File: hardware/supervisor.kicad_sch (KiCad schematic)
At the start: 39 parts, among them U5 STM32L4P5RET6, U6 MCP2562-H-SN, Y1 Crystal_GND24

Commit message: Dimensions compress, routing
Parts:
- removed 120_JP1: Jumper_NC_Small, Jumper:SolderJumper-2_P1.3mm_Open_RoundedPad1.0x1.5mm, symbol Jumper:Jumper_2_Open
- removed C10, C12, C14, C15, C18, C7, C8, C9: 100nF, Capacitor_SMD:C_0603_1608Metric_Pad1.08x0.95mm_HandSolder, symbol Device:C
- removed C6: 1uF, Capacitor_SMD:C_0603_1608Metric_Pad1.08x0.95mm_HandSolder, symbol Device:C
- removed D2: PESD2CAN.215, Package_TO_SOT_SMD:SOT-23, symbol Device:D_TVS_Dual_AAC
- removed L1: 10u, Inductor_SMD:L_0805_2012Metric, symbol Device:L
- removed R13: 120R, Resistor_SMD:R_0603_1608Metric_Pad0.98x0.95mm_HandSolder, symbol Device:R_Small
- removed U6: MCP2562-H-SN, Package_SO:SOIC-8_3.9x4.9mm_P1.27mm, symbol Interface_CAN_LIN:MCP2562-H-SN
- Y1: value Crystal_GND24 -> 8MHz 3225 Crystal
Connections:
- net (CAN_RX)+ renamed CAN_RX
- net (CAN_TX)- renamed CAN_TX
- net XTAL1: no longer names the net of C11.1, U5.5 (PH0-OSC_IN), Y1.1
- net XTAL2: no longer names the net of C13.1, U5.6 (PH1-OSC_OUT), Y1.3
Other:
- added sheet CAN_comm (can.kicad_sch)
- added sheet uC power decoupling (decoupling.kicad_sch)
- note removed: "8Mhz"
- note removed: "sensor 1,2,3 Pins: 24, 25, 37"
- note removed: "those are just in case, brake pressure read from data acquisition card frames"
- note removed: "uC Power supply decoupling"
- moved on the sheet: C11, C13, D16, D17, D18, D6, JP1, JP2, R11, R12, R2, R20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

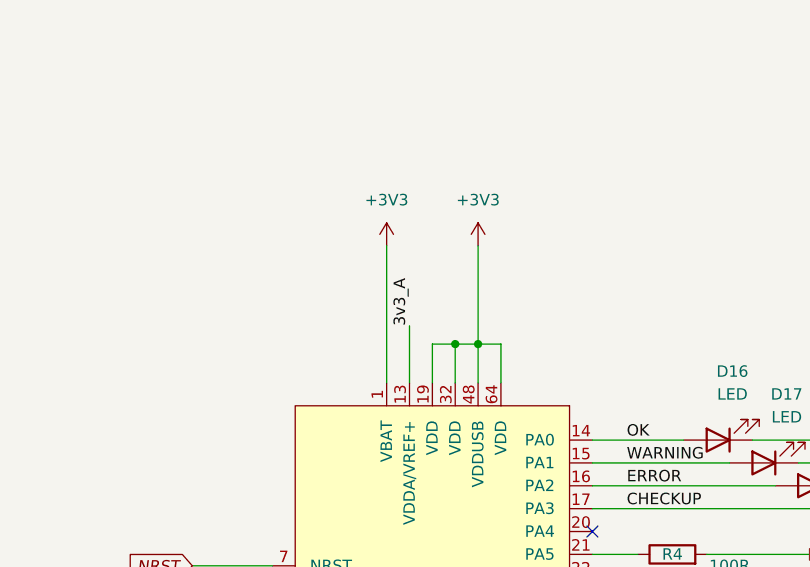
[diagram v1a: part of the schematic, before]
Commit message: replace RES2 input to actuator relai
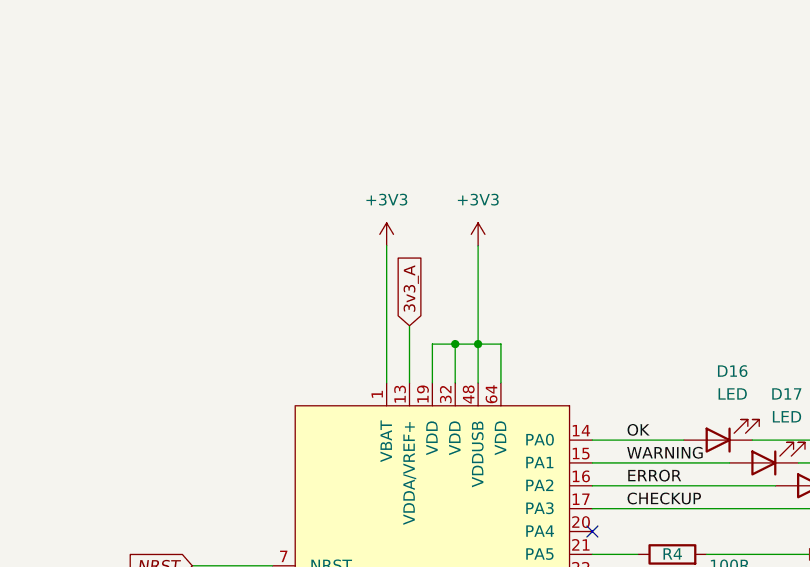
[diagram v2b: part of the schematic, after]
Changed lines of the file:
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@@
     (effects (font (size 1.27 1.27)) (justify left bottom))
   )
-  (label "3v3_A" (at 137.16 54.61 90) (fields_autoplaced)
-    (effects (font (size 1.27 1.27)) (justify left bottom))
+  (global_label "3v3_A" (shape input) (at 137.16 54.61 90) (fields_autoplaced)
+    (effects (font (size 1.27 1.27)) (justify left))
+    (property "Intersheetrefs" "${INTERSHEET_REFS}" (at 137.16 46.2614 90)
+      (effects (font (size 1.27 1.27)) (justify left) hide)
+    )
   )
   (global_label "NRST" (shape input) (at 113.03 81.28 180) (fields_autoplaced)

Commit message: changed pcb version
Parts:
- removed JP1, JP2: Jumper_NC_Small, Jumper:SolderJumper-2_P1.3mm_Open_RoundedPad1.0x1.5mm, symbol Jumper:Jumper_2_Open
- removed R11, R33, R6: 100R, Resistor_SMD:R_0603_1608Metric_Pad0.98x0.95mm_HandSolder, symbol Device:R
- removed R29, R49, R50: 10k, Resistor_SMD:R_0603_1608Metric_Pad0.98x0.95mm_HandSolder, symbol Device:R_Small
- added 120_JP1: Jumper_NC_Small, Connector_PinHeader_2.54mm:PinHeader_1x02_P2.54mm_Vertical, symbol Jumper:Jumper_2_Open
- added C10, C12, C14, C18, C7, C8, C9: 100nF, Capacitor_SMD:C_0603_1608Metric_Pad1.08x0.95mm_HandSolder, symbol Device:C
- added C15: 100nF, Capacitor_SMD:C_0805_2012Metric_Pad1.18x1.45mm_HandSolder, symbol Device:C
- added C6: 1uF, Capacitor_SMD:C_0603_1608Metric_Pad1.08x0.95mm_HandSolder, symbol Device:C
- added D2: PESD2CAN.215, Package_TO_SOT_SMD:SOT-23, symbol Device:D_TVS_Dual_AAC
- added L1: 10u, Inductor_SMD:L_0805_2012Metric, symbol Device:L
- added R13: 120R, Resistor_SMD:R_0603_1608Metric_Pad0.98x0.95mm_HandSolder, symbol Device:R_Small
- added U6: MCP2562-H-SN, Package_SO:SOIC-8_3.9x4.9mm_P1.27mm, symbol Interface_CAN_LIN:MCP2562-H-SN
- R2, R20, R4, R5: value 100R -> 2.2k
- Y1: value 8MHz 3225 Crystal -> Crystal_GND24
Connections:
- net +3V3: now also C10.1, C12.1, C14.1, C18.1, C6.1, C8.1, C9.1, L1.1, U6.5 (Vio)
- net 3v3_A: now also C7.1, L1.2
- net GND: now also C10.2, C12.2, C14.2, C15.2, C18.2, C6.2, C7.2, C8.2, C9.2, D2.3 (common), U6.2 (VSS), U6.8 (STBY)
- net SPARE1: now also U5.26 (PB0)
- net SPARE2: now also U5.27 (PB1)
- net XTAL1: now reaches C11.1, U5.5 (PH0-OSC_IN), Y1.1
- net XTAL2: now reaches C13.1, U5.6 (PH1-OSC_OUT), Y1.3
- net at R5.1: now also U5.22 (PA6); no longer U5.27 (PB1)
- net AIR_SPARE: no longer names the net of U5.11 (PC3)
- net CAN_RX renamed (CAN_RX)+
- net (CAN_RX)+: now also U6.4 (RXD)
- net CAN_TX renamed (CAN_TX)-
- net (CAN_TX)-: now also U6.1 (TXD)
- net TS_ON_EXT_P renamed AS_DRIVING_MODE
- new net: 120_JP1.2 (B), R13.1
- new net +5V: C15.1, U6.3 (VDD)
- new net CAN+: 120_JP1.1 (A), D2.2 (A2), U6.7 (CANH)
- new net CAN-: D2.1 (A1), R13.2, U6.6 (CANL)
- no-connect marks 26 -> 30
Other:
- removed sheet CAN_comm
- removed sheet uC power decoupling
- note added: "8Mhz"
- note added: "sensor 1,2,3 Pins: 24, 25, 37"
- note added: "those are just in case, brake pressure read from data acquisition card frames"
- note added: "uC Power supply decoupling"
- note removed: "//warning: spares changed from PB0 PB1 to PC4 PC5"
- moved on the sheet: C11, C13, D16, D17, D18, D6, R12, R2, R20, R35, R36, R37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

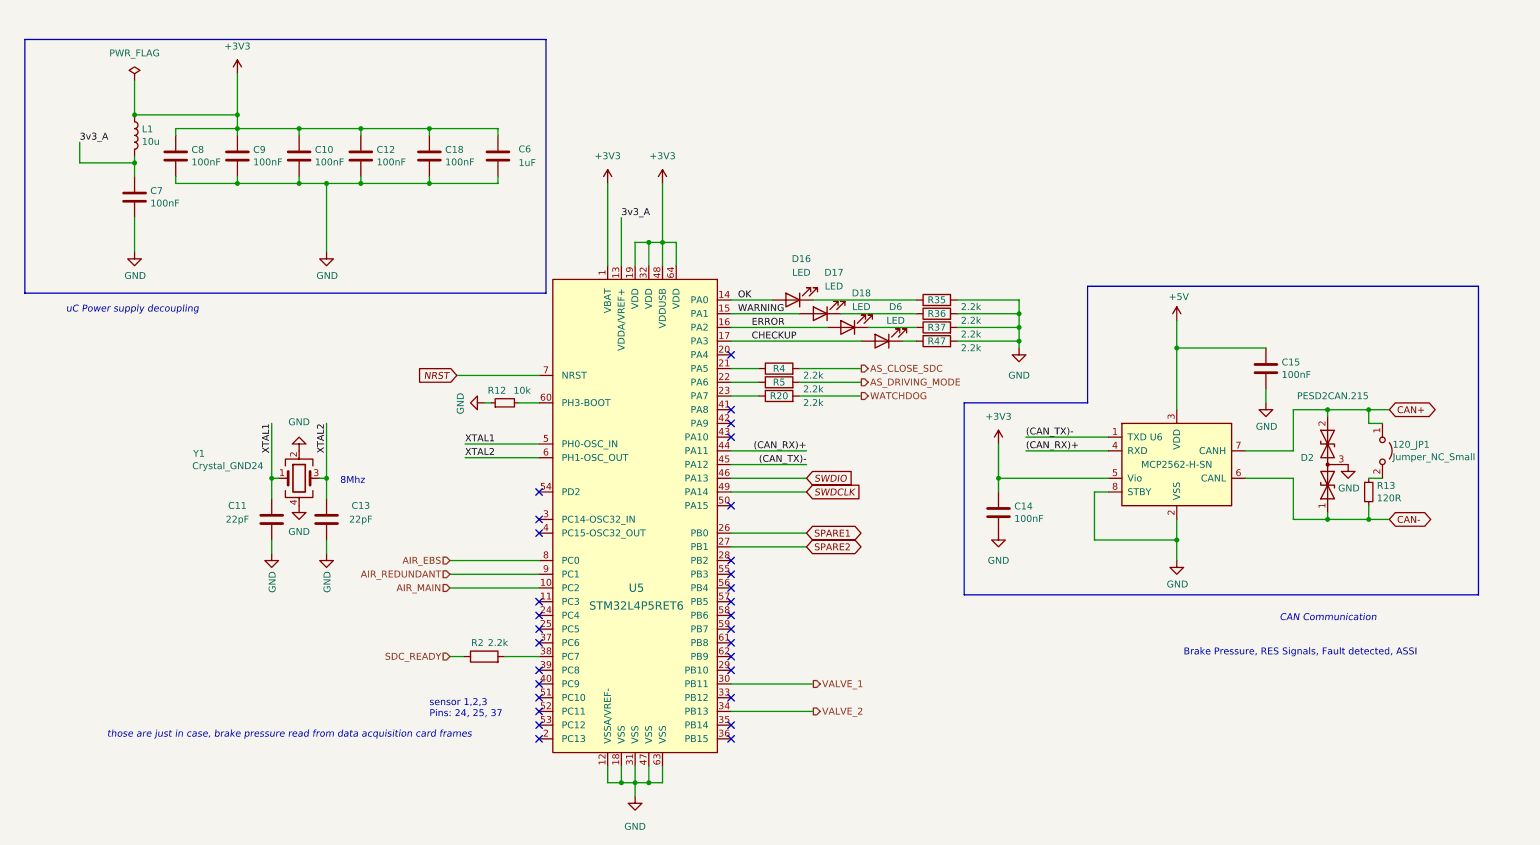
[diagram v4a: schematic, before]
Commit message: Schematic redesign for 23 rules, new pressure buffer, protection fix
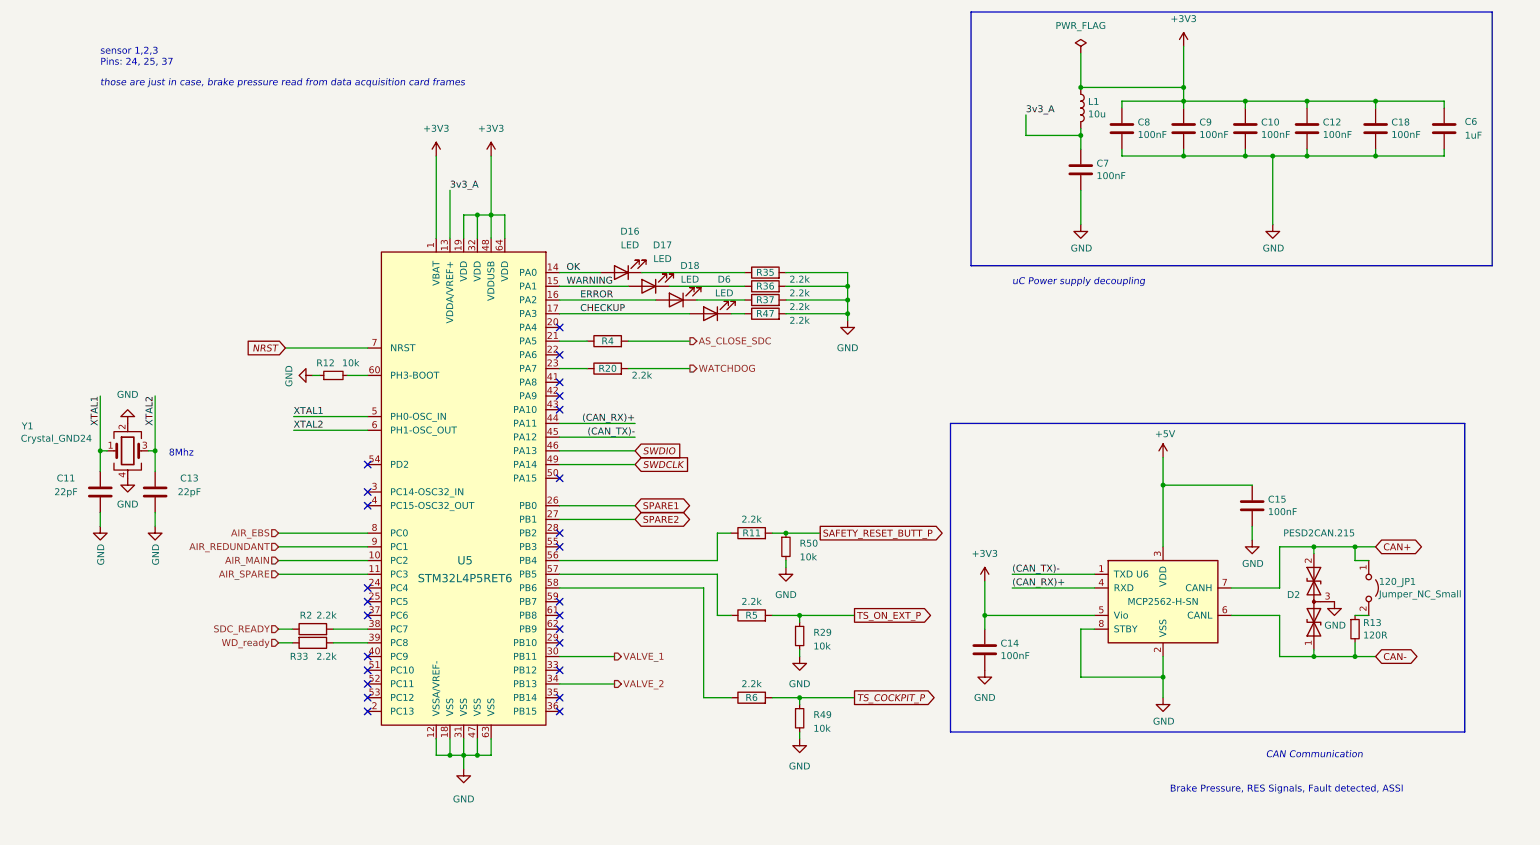
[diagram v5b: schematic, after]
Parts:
- added R11, R33, R6: 2.2k, Resistor_SMD:R_0603_1608Metric_Pad0.98x0.95mm_HandSolder, symbol Device:R
- added R29, R49, R50: 10k, Resistor_SMD:R_0603_1608Metric_Pad0.98x0.95mm_HandSolder, symbol Device:R_Small
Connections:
- net GND: now also R29.2, R49.2, R50.2
- net at R5.1: now also U5.57 (PB5); no longer U5.22 (PA6)
- net AIR_SPARE: now reaches U5.11 (PC3)
- net at U5.39 (PC8): now also R33.1
- net at U5.56 (PB4): now also R11.1
- net at U5.58 (PB6): now also R6.1
- net AS_DRIVING_MODE renamed TS_ON_EXT_P
- net TS_ON_EXT_P: now also R29.1
- new net SAFETY_RESET_BUTT_P: R11.2, R50.1
- new net TS_COCKPIT_P: R49.1, R6.2
- new net WD_ready: R33.2
- no-connect marks 30 -> 26
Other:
- moved on the sheet: 120_JP1, C10, C11, C12, C13, C14, C15, C18, C6, C7, C8, C9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

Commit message: WIP revision 2 layout refinement
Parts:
- C15: footprint Capacitor_SMD:C_0805_2012Metric_Pad1.18x1.45mm_HandSolder -> Capacitor_SMD:C_0603_1608Metric_Pad1.08x0.95mm_HandSolder
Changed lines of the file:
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@@
       (effects (font (size 1.27 1.27)) (justify left))
     )
-    (property "Footprint" "Capacitor_SMD:C_0805_2012Metric_Pad1.18x1.45mm_HandSolder" (at 242.2652 111.76 0)
+    (property "Footprint" "Capacitor_SMD:C_0603_1608Metric_Pad1.08x0.95mm_HandSolder" (at 242.2652 111.76 0)
       (effects (font (size 1.27 1.27)) hide)
     )

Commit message: 2.0 layot wip, each sections placed
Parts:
- added JP2, JP3: Jumper_NC_Small, Jumper:SolderJumper-2_P1.3mm_Open_RoundedPad1.0x1.5mm, symbol Jumper:Jumper_2_Open
- 120_JP1: footprint Connector_PinHeader_2.54mm:PinHeader_1x02_P2.54mm_Vertical -> Jumper:SolderJumper-2_P1.3mm_Open_RoundedPad1.0x1.5mm
- R11, R2, R33, R5, R6: value 2.2k -> 100R
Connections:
- net SPARE1: now also JP2.2 (B); no longer U5.26 (PB0)
- net SPARE2: now also JP3.1 (A); no longer U5.27 (PB1)
- new net: JP3.2 (B), U5.27 (PB1)
- new net: JP2.1 (A), U5.26 (PB0)
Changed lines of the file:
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@@
+    (stroke (width 0) (type default))
+  )
+  (wire (pts (xy 125.73 110.49) (xy 130.81 110.49))
     (stroke (width 0) (type default))
   )
@@
     (stroke (width 0) (type default))
   )
+  (wire (pts (xy 113.03 110.49) (xy 115.57 110.49))
+    (stroke (width 0) (type default))
+  )
+  (wire (pts (xy 113.03 107.95) (xy 115.57 107.95))
+    (stroke (width 0) (type default))
+  )
   (wire (pts (xy 63.754 93.98) (xy 77.47 93.98))
     (stroke (width 0) (type default))
@@
     (stroke (width 0) (type default))
   )
-  (wire (pts (xy 113.03 107.95) (xy 127 107.95))
-    (stroke (width 0) (type default))
-  )
   (wire (pts (xy 260.35 115.57) (xy 260.35 118.11))
     (stroke (width 0) (type default))
@@
     (stroke (width 0) (type default))
   )
+  (wire (pts (xy 125.73 107.95) (xy 130.81 107.95))
+    (stroke (width 0) (type default))
+  )
   (wire (pts (xy 228.6 22.86) (xy 228.6 30.48))
     (stroke (width 0) (type default))
@@
   )
   (wire (pts (xy 276.86 41.91) (xy 276.86 43.18))
-    (stroke (width 0) (type default))
-  )
-  (wire (pts (xy 113.03 110.49) (xy 127 110.49))
     (stroke (width 0) (type default))
   )
@@
     )
   )
-  (global_label "SPARE1" (shape bidirectional) (at 127 107.95 0) (fields_autoplaced)
+  (global_label "SPARE1" (shape bidirectional) (at 130.81 107.95 0) (fields_autoplaced)
     (effects (font (size 1.27 1.27)) (justify left))
-    (property "Intersheetrefs" "${INTERSHEET_REFS}" (at 136.6098 107.8706 0)
+    (property "Intersheetrefs" "${INTERSHEET_REFS}" (at 140.4198 107.8706 0)
       (effects (font (size 1.27 1.27)) (justify left) hide)
     )
@@
     )
   )
-  (global_label "SPARE2" (shape bidirectional) (at 127 110.49 0) (fields_autoplaced)
+  (global_label "SPARE2" (shape bidirectional) (at 130.81 110.49 0) (fields_autoplaced)
     (effects (font (size 1.27 1.27)) (justify left))
-    (property "Intersheetrefs" "${INTERSHEET_REFS}" (at 136.6098 110.4106 0)
+    (property "Intersheetrefs" "${INTERSHEET_REFS}" (at 140.4198 110.4106 0)
       (effects (font (size 1.27 1.27)) (justify left) hide)
     )
@@
       (effects (font (size 1.27 1.27)))
     )
-    (property "Value" "2.2k" (at 69.85 135.89 90)
+    (property "Value" "100R" (at 69.85 135.89 90)
       (effects (font (size 1.27 1.27)))
     )
@@
     )
   )
+  (symbol (lib_id "Jumper:Jumper_2_Open") (at 120.65 110.49 180) (unit 1)
+    (in_bom yes) (on_board yes) (dnp no)
+    (property "Reference" "JP3" (at 121.8184 112.3696 90)
+      (effects (font (size 1.27 1.27)) (justify left))
+    )
+    (property "Value" "Jumper_NC_Small" (at 119.507 112.3696 90)
+      (effects (font (size 1.27 1.27)) (justify left) hide)
+    )
+    (property "Footprint" "Jumper:SolderJumper-2_P1.3mm_Open_RoundedPad1.0x1.5mm" (at 120.65 110.49 0)
+      (effects (font (size 1.27 1.27)) hide)
+    )
+    (property "Datasheet" "~" (at 120.65 110.49 0)
+      (effects (font (size 1.27 1.27)) hide)
+    )
+    (pin "1")
+    (pin "2")
+    (instances
+      (project "PUTM_DV_EBS_2023"
+        (path "/d921fbb5-521e-405d-bdec-f40195adfa1c/bbd4f989-bc6f-4d23-b657-5429a2409e1d"
+          (reference "JP3") (unit 1)
+        )
+      )
+    )
+  )
   (symbol (lib_id "Device:R") (at 148.59 128.27 90) (unit 1)
     (in_bom yes) (on_board yes) (dnp no)
@@
       (effects (font (size 1.27 1.27)))
     )
-    (property "Value" "2.2k" (at 148.59 125.73 90)
+    (property "Value" "100R" (at 148.59 125.73 90)
       (effects (font (size 1.27 1.27)))
     )
@@
     )
     (property "Value" "Jumper_NC_Small" (at 264.7696 124.333 90)
-      (effects (font (size 1.27 1.27)) (justify left))
-    )
-    (property "Footprint" "Connector_PinHeader_2.54mm:PinHeader_1x02_P2.54mm_Vertical" (at 262.89 123.19 0)
+      (effects (font (size 1.27 1.27)) (justify left) hide)
+    )
+    (property "Footprint" "Jumper:SolderJumper-2_P1.3mm_Open_RoundedPad1.0x1.5mm" (at 262.89 123.19 0)
       (effects (font (size 1.27 1.27)) hide)
     )
@@
       (effects (font (size 1.27 1.27)))
     )
-    (property "Value" "2.2k" (at 148.59 110.49 90)
+    (property "Value" "100R" (at 148.59 110.49 90)
       (effects (font (size 1.27 1.27)))
     )
@@
     )
   )
+  (symbol (lib_id "Jumper:Jumper_2_Open") (at 120.65 107.95 0) (unit 1)
+    (in_bom yes) (on_board yes) (dnp no)
+    (property "Reference" "JP2" (at 119.4816 106.0704 90)
+      (effects (font (size 1.27 1.27)) (justify left))
+    )
+    (property "Value" "Jumper_NC_Small" (at 121.793 106.0704 90)
+      (effects (font (size 1.27 1.27)) (justify left) hide)
+    )
+    (property "Footprint" "Jumper:SolderJumper-2_P1.3mm_Open_RoundedPad1.0x1.5mm" (at 120.65 107.95 0)
+      (effects (font (size 1.27 1.27)) hide)
+    )
+    (property "Datasheet" "~" (at 120.65 107.95 0)
+      (effects (font (size 1.27 1.27)) hide)
+    )
+    (pin "1")
+    (pin "2")
+    (instances
+      (project "PUTM_DV_EBS_2023"
+        (path "/d921fbb5-521e-405d-bdec-f40195adfa1c/bbd4f989-bc6f-4d23-b657-5429a2409e1d"
+          (reference "JP2") (unit 1)
+        )
+      )
+    )
+  )
   (symbol (lib_id "Device:R_Small") (at 71.12 83.82 90) (unit 1)
     (in_bom yes) (on_board yes) (dnp no)
@@
       (effects (font (size 1.27 1.27)))
     )
-    (property "Value" "2.2k" (at 69.85 128.27 90)
+    (property "Value" "100R" (at 69.85 128.27 90)
       (effects (font (size 1.27 1.27)))
     )
@@
       (effects (font (size 1.27 1.27)))
     )
-    (property "Value" "2.2k" (at 148.59 140.97 90)
-      (effects (font (size 1.27 1.27)))
-    )
+    (property "Value" "100R" (at 148.59 140.97 90)
+      (effects (font (size 1.27 1.27)))
+    )

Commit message: WIP 1.1 routing
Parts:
- removed JP3: Jumper_NC_Small, Jumper:SolderJumper-2_P1.3mm_Open_RoundedPad1.0x1.5mm, symbol Jumper:Jumper_2_Open
- added JP1: Jumper_NC_Small, Jumper:SolderJumper-2_P1.3mm_Open_RoundedPad1.0x1.5mm, symbol Jumper:Jumper_2_Open
- R20, R4: value 2.2k -> 100R
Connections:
- net SPARE1: now also JP1.2 (B); no longer JP2.2 (B)
- net SPARE2: now also JP2.1 (A)
- net at U5.27 (PB1): now also R5.1
- net at U5.57 (PB5): no longer R5.1
- net at U5.24 (PC4): now also JP1.1 (A)
- net at U5.25 (PC5): now also JP2.2 (B)
- net at U5.26 (PB0): now also R11.1; no longer JP2.1 (A)
- net at U5.28 (PB2): now also R6.1
- net at U5.56 (PB4): no longer R11.1
- net at U5.58 (PB6): no longer R6.1
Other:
- note added: "//warning: spares changed from PB0 PB1 to PC4 PC5"
- moved on the sheet: R11, R29, R49, R5, R50, R6
